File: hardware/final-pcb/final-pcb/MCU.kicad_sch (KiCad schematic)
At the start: 1 part, among them U2 STM32L496ZGT6

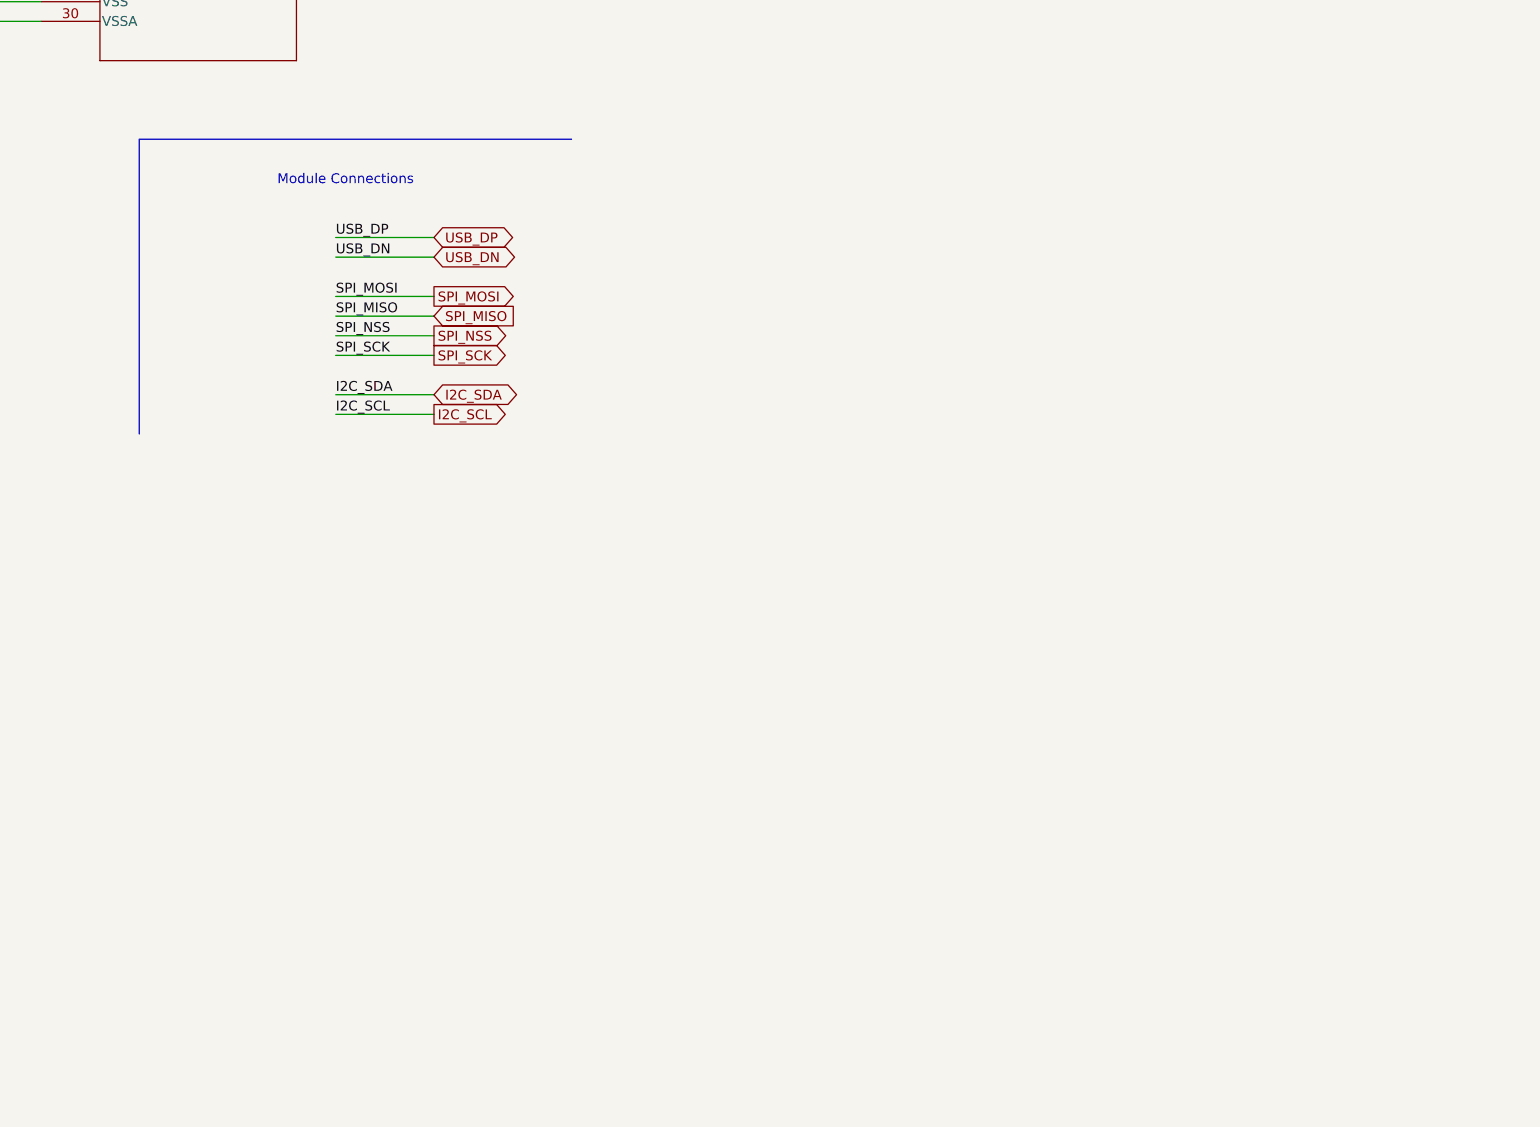
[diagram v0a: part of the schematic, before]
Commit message: Update sizes of schematics
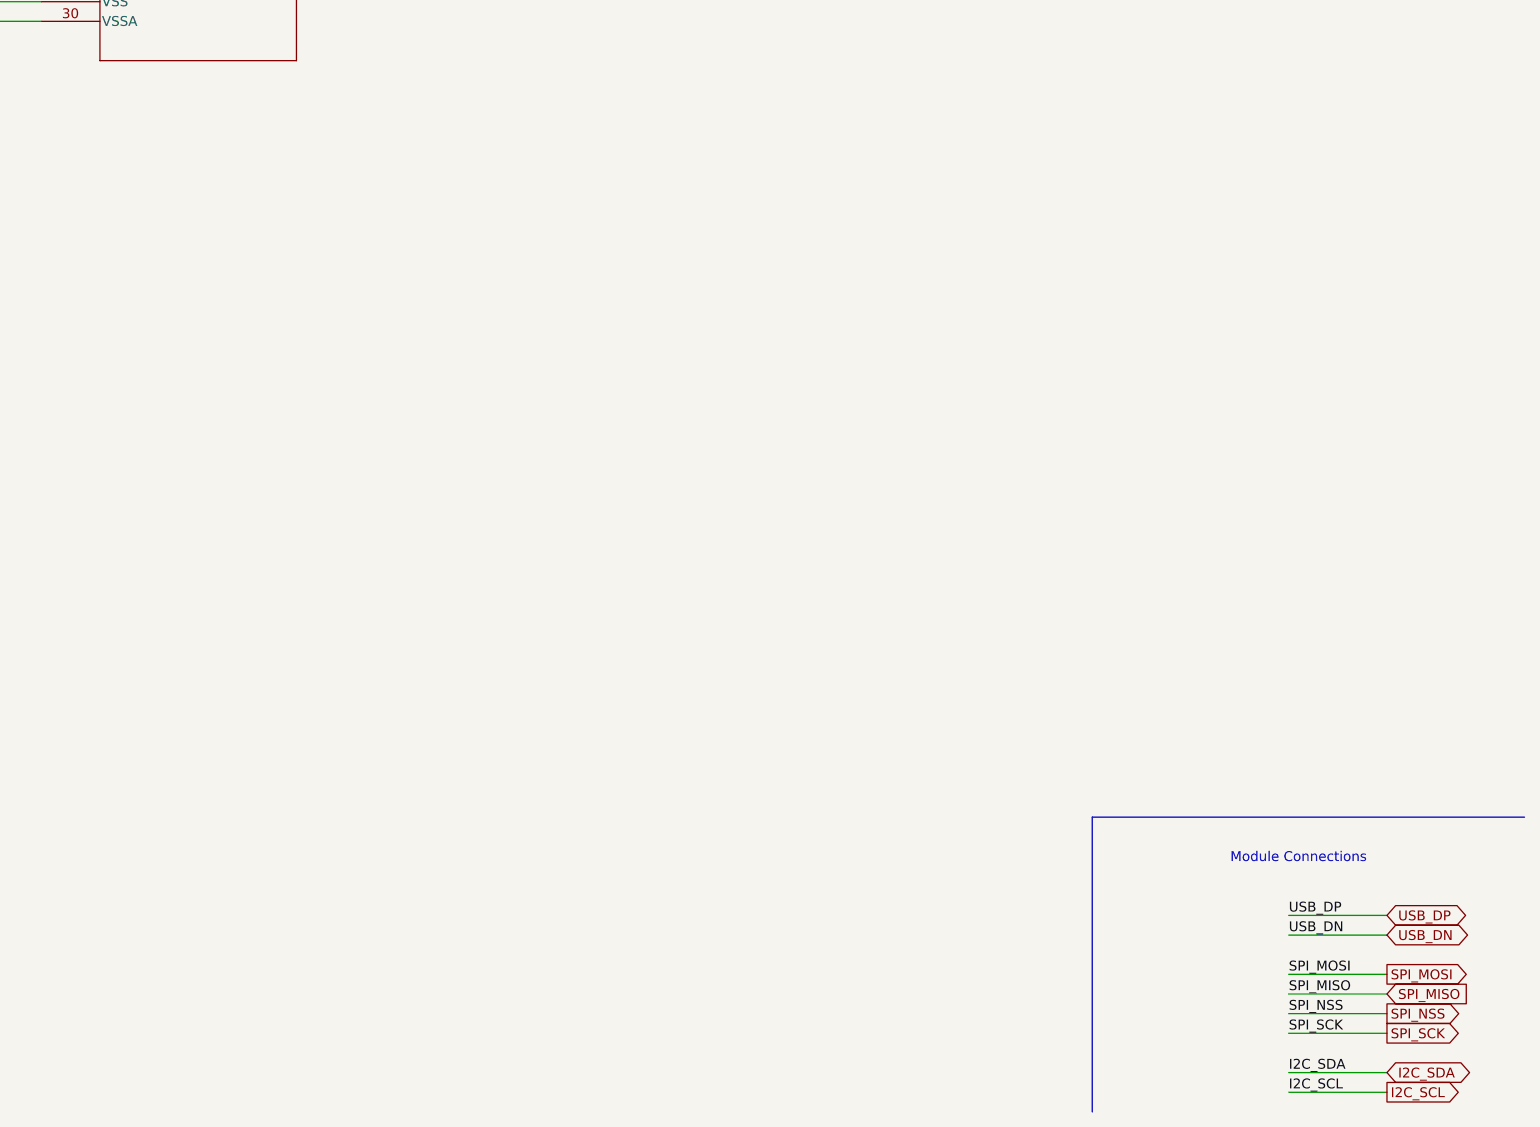
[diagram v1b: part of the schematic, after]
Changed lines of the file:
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@@
 	(generator "eeschema")
 	(generator_version "8.0")
-	(paper "A4")
+	(paper "A3")
 	(junction
 		(at 203.2 99.06)
@@
 	(wire
 		(pts
-			(xy 254 152.4) (xy 266.7 152.4)
+			(xy 377.19 240.03) (xy 389.89 240.03)
 		)
 		(stroke
@@
 	(wire
 		(pts
-			(xy 254 139.7) (xy 266.7 139.7)
-		)
-		(stroke
-			(width 0)
-			(type default)
-		)
-	)
-	(wire
-		(pts
-			(xy 254 154.94) (xy 266.7 154.94)
+			(xy 377.19 227.33) (xy 389.89 227.33)
+		)
+		(stroke
+			(width 0)
+			(type default)
+		)
+	)
+	(wire
+		(pts
+			(xy 377.19 242.57) (xy 389.89 242.57)
 		)
 		(stroke
@@
 	(wire
 		(pts
-			(xy 254 149.86) (xy 266.7 149.86)
+			(xy 377.19 237.49) (xy 389.89 237.49)
 		)
 		(stroke
@@
 	(polyline
 		(pts
-			(xy 284.48 127) (xy 228.6 127)
+			(xy 407.67 214.63) (xy 351.79 214.63)
 		)
 		(stroke
@@
 	(wire
 		(pts
-			(xy 254 147.32) (xy 266.7 147.32)
+			(xy 377.19 234.95) (xy 389.89 234.95)
 		)
 		(stroke
@@
 	(wire
 		(pts
-			(xy 254 142.24) (xy 266.7 142.24)
+			(xy 377.19 229.87) (xy 389.89 229.87)
 		)
 		(stroke
@@
 	(polyline
 		(pts
-			(xy 228.6 127) (xy 228.6 165.1)
+			(xy 351.79 214.63) (xy 351.79 252.73)
 		)
 		(stroke
@@
 	(wire
 		(pts
-			(xy 254 162.56) (xy 266.7 162.56)
+			(xy 377.19 250.19) (xy 389.89 250.19)
 		)
 		(stroke
@@
 	(wire
 		(pts
-			(xy 254 160.02) (xy 266.7 160.02)
+			(xy 377.19 247.65) (xy 389.89 247.65)
 		)
 		(stroke
@@
 	(text "Module Connections"
 		(exclude_from_sim no)
-		(at 255.27 132.334 0)
+		(at 378.46 219.964 0)
 		(effects
 			(font
@@
 	)
 	(label "SPI_MISO"
-		(at 254 149.86 0)
+		(at 377.19 237.49 0)
 		(fields_autoplaced yes)
 		(effects
@@
 	)
 	(label "I2C_SDA"
-		(at 254 160.02 0)
+		(at 377.19 247.65 0)
 		(fields_autoplaced yes)
 		(effects
@@
 	)
 	(label "I2C_SCL"
-		(at 254 162.56 0)
+		(at 377.19 250.19 0)
 		(fields_autoplaced yes)
 		(effects
@@
 	)
 	(label "USB_DN"
-		(at 254 142.24 0)
+		(at 377.19 229.87 0)
 		(fields_autoplaced yes)
 		(effects
@@
 	)
 	(label "SPI_NSS"
-		(at 254 152.4 0)
+		(at 377.19 240.03 0)
 		(fields_autoplaced yes)
 		(effects
@@
 	)
 	(label "USB_DP"
-		(at 254 139.7 0)
+		(at 377.19 227.33 0)
 		(fields_autoplaced yes)
 		(effects
@@
 	)
 	(label "SPI_SCK"
-		(at 254 154.94 0)
+		(at 377.19 242.57 0)
 		(fields_autoplaced yes)
 		(effects
@@
 	)
 	(label "SPI_MOSI"
-		(at 254 147.32 0)
+		(at 377.19 234.95 0)
 		(fields_autoplaced yes)
 		(effects
@@
 	(global_label "SPI_SCK"
 		(shape output)
-		(at 266.7 154.94 0)
+		(at 389.89 242.57 0)
 		(fields_autoplaced yes)
 		(effects
@@
 		)
 		(property "Intersheetrefs" "${INTERSHEET_REFS}"
-			(at 277.4866 154.94 0)
+			(at 400.6766 242.57 0)
 			(effects
 				(font
@@
 	(global_label "SPI_MISO"
 		(shape input)
-		(at 266.7 149.86 0)
+		(at 389.89 237.49 0)
 		(fields_autoplaced yes)
 		(effects
@@
 		)
 		(property "Intersheetrefs" "${INTERSHEET_REFS}"
-			(at 278.3333 149.86 0)
+			(at 401.5233 237.49 0)
 			(effects
 				(font
@@
 	(global_label "USB_DN"
 		(shape bidirectional)
-		(at 266.7 142.24 0)
+		(at 389.89 229.87 0)
 		(fields_autoplaced yes)
 		(effects
@@
 		)
 		(property "Intersheetrefs" "${INTERSHEET_REFS}"
-			(at 277.0633 142.24 0)
+			(at 400.2533 229.87 0)
 			(effects
 				(font
@@
 	(global_label "I2C_SCL"
 		(shape output)
-		(at 266.7 162.56 0)
+		(at 389.89 250.19 0)
 		(fields_autoplaced yes)
 		(effects
@@
 		)
 		(property "Intersheetrefs" "${INTERSHEET_REFS}"
-			(at 277.2447 162.56 0)
+			(at 400.4347 250.19 0)
 			(effects
 				(font
@@
 	(global_label "USB_DP"
 		(shape bidirectional)
-		(at 266.7 139.7 0)
+		(at 389.89 227.33 0)
 		(fields_autoplaced yes)
 		(effects
@@
 		)
 		(property "Intersheetrefs" "${INTERSHEET_REFS}"
-			(at 277.0028 139.7 0)
+			(at 400.1928 227.33 0)
 			(effects
 				(font
@@
 	(global_label "SPI_NSS"
 		(shape output)
-		(at 266.7 152.4 0)
+		(at 389.89 240.03 0)
 		(fields_autoplaced yes)
 		(effects
@@
 		)
 		(property "Intersheetrefs" "${INTERSHEET_REFS}"
-			(at 277.4866 152.4 0)
+			(at 400.6766 240.03 0)
 			(effects
 				(font
@@
 	(global_label "SPI_MOSI"
 		(shape output)
-		(at 266.7 147.32 0)
+		(at 389.89 234.95 0)
 		(fields_autoplaced yes)
 		(effects
@@
 		)
 		(property "Intersheetrefs" "${INTERSHEET_REFS}"
-			(at 278.3333 147.32 0)
+			(at 401.5233 234.95 0)
 			(effects
 				(font
@@
 	(global_label "I2C_SDA"
 		(shape bidirectional)
-		(at 266.7 160.02 0)
+		(at 389.89 247.65 0)
 		(fields_autoplaced yes)
 		(effects
@@
 		)
 		(property "Intersheetrefs" "${INTERSHEET_REFS}"
-			(at 277.3052 160.02 0)
-			(effects
-				(font
+			(at 400.4952 247.65 0)
+			(effects
+				(font

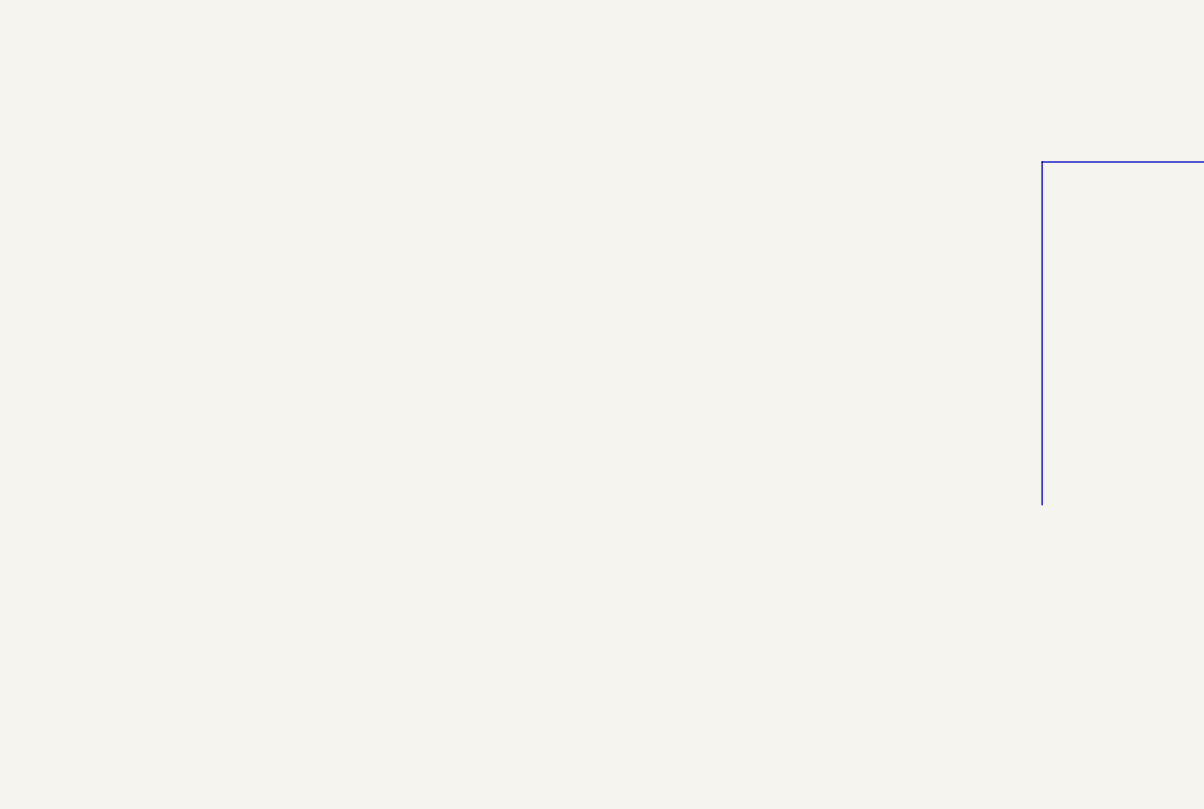
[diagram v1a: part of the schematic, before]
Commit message: Add syms, footprints, 3dmodels for ADS and LTC boards
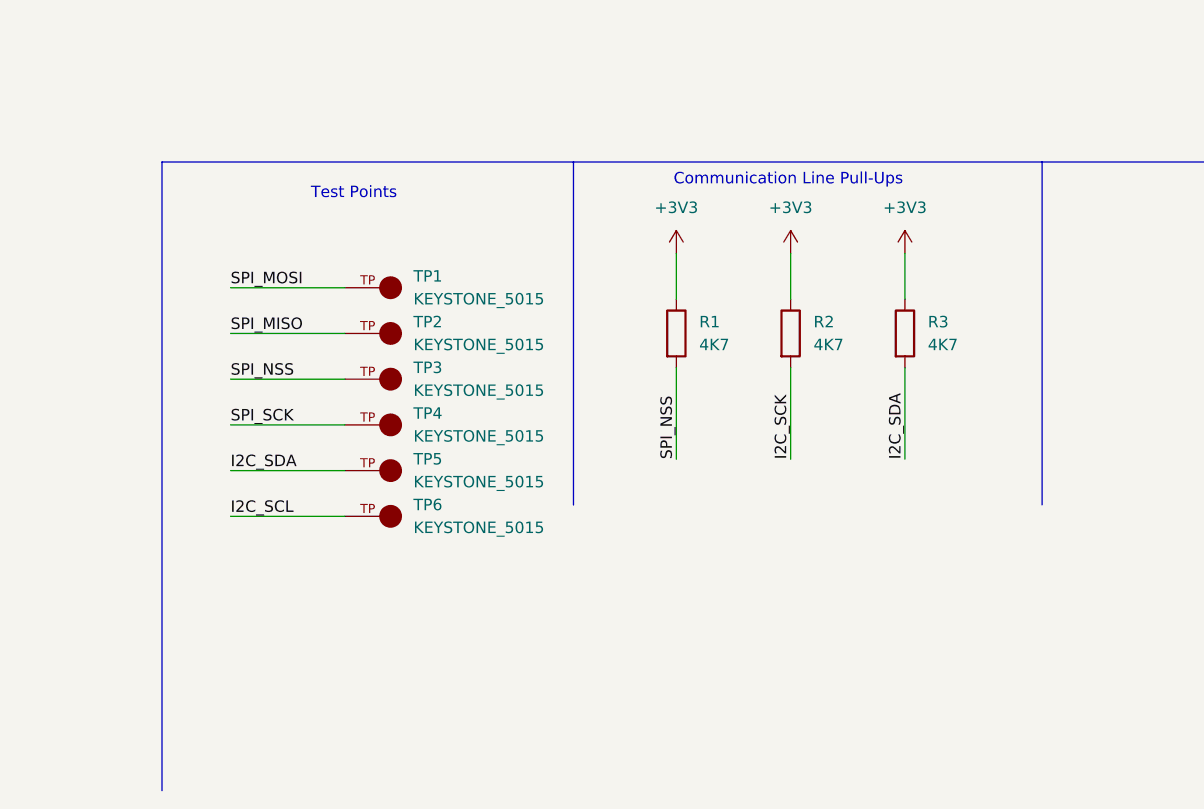
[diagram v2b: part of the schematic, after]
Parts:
- added R1, R2, R3: 4K7, symbol hands-emg-lib:R
- added TP1, TP2, TP3, TP4, TP5, TP6: KEYSTONE_5015, hands-emg-lib:KEYSTONE_5015, symbol hands-emg-lib:KEYSTONE_5015
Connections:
- net I2C_SCL: now also TP6.TP
- net I2C_SDA: now also R3.2, TP5.TP
- net SPI_MISO: now also TP2.TP
- net SPI_MOSI: now also TP1.TP
- net SPI_NSS: now also R1.2, TP3.TP
- net SPI_SCK: now also TP4.TP
- new net +3V3: R1.1, R2.1, R3.1
- new net I2C_SCK: R2.2
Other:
- note added: "Communication Line Pull-Ups"
- note added: "Test Points"
- company: (none) -> San Diego State University
- title: (none) -> Microcontroller
